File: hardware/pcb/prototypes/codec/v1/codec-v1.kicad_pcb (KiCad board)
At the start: 2 copper layers, 40.6 x 25.4 mm, 18 parts, among them J1 IN_1, J2 IN_2, J3 DATA_PINS, J4 PWR, J5 OUT_1, J6 OUT_2, U1 TAC5212

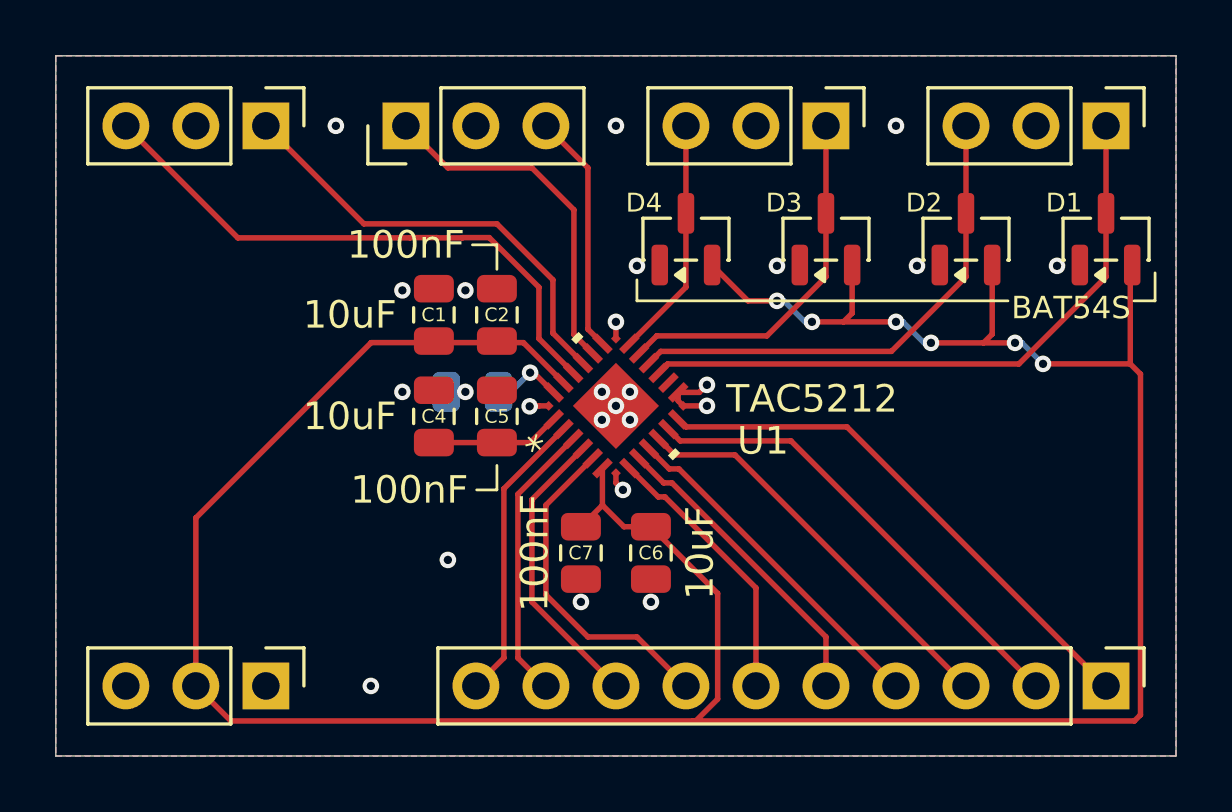
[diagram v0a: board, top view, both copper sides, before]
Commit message: adjust layout and silkscreen
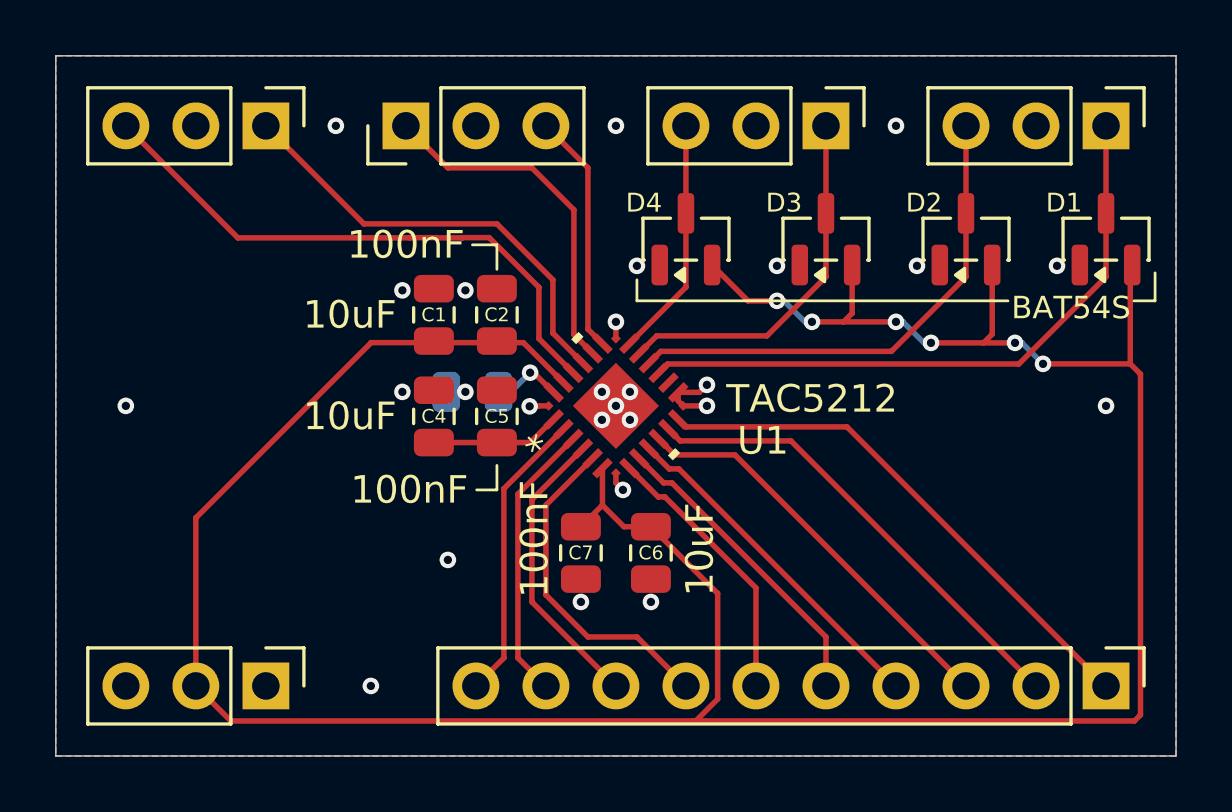
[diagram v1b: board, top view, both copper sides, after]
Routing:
- net GNDA: vias 25 -> 27
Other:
- board text added: "GND +3V3 GND"
- board text added: "IN 1+ GND IN 1-"
- board text added: "IN 2+ GND IN 2-"
- board text added: "OUT 1- GND OUT 1+"
- board text added: "OUT 2+ GND OUT 2-"
- board text added: "SPI CS SPI POCI GPIO 2 CCLK SPI PICO SPI SCLK I2S DIN I2S DOUT I2S FSYNC I2S BCLK"
